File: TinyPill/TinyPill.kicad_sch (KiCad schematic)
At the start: 25 parts

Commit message: Finish GPIO selection
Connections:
- net UART_TX: now reaches U?.12 (PA2)
- net UART_RX: now reaches U?.13 (PA3)
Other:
- note added: "MCU and USB-C 2.0"
- note added: "Power Supply"
- note added: "TinyPill"
- company: (none) -> John Trachte
- title: (none) -> TinyPill Schematic
- moved on the sheet: C?, D?, FB?, J?, R?, SW?, U?

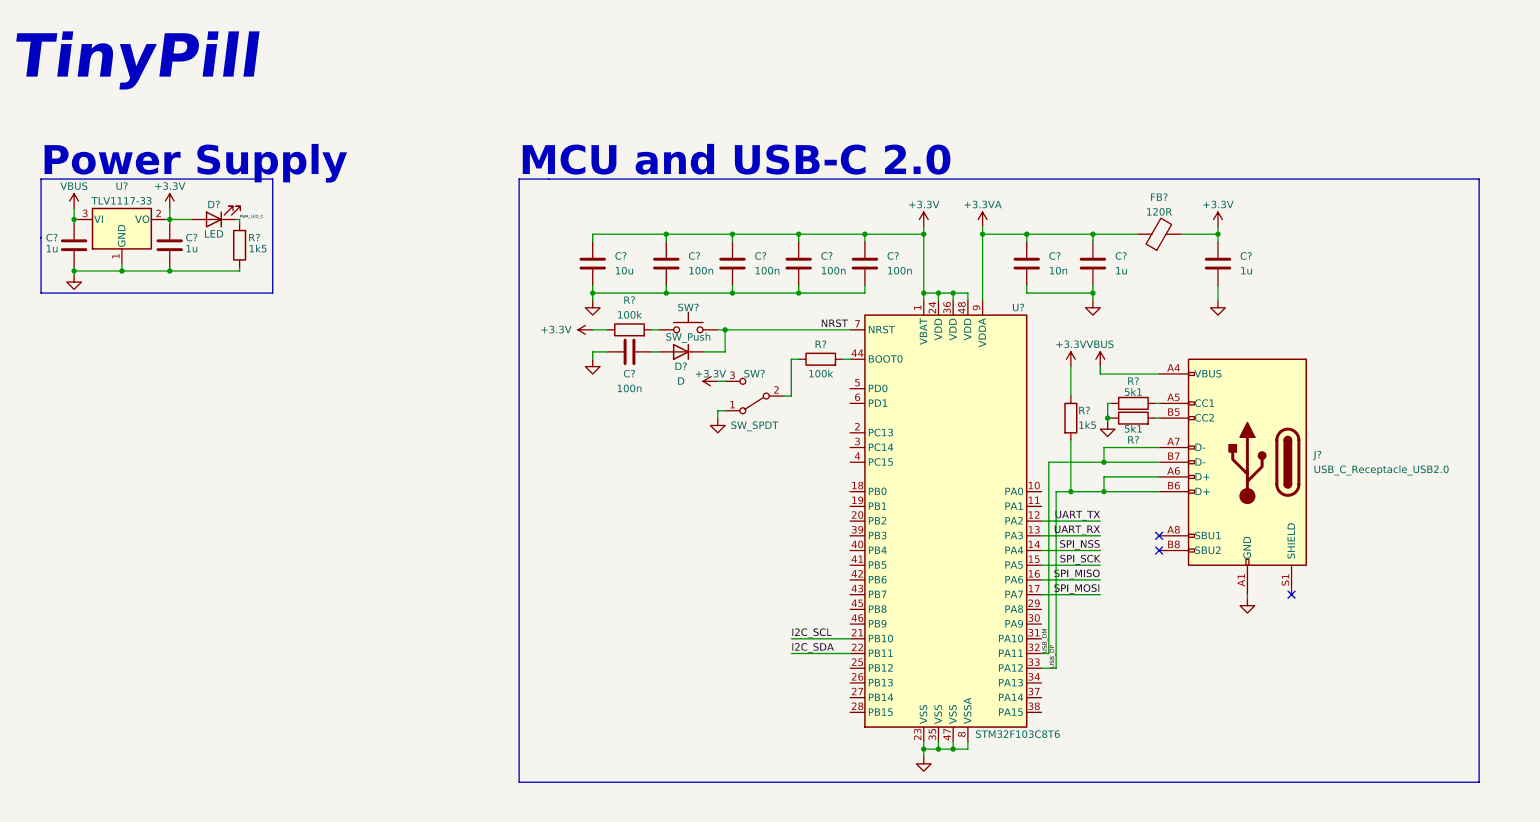
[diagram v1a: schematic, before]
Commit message: Annotations, footprint assignment
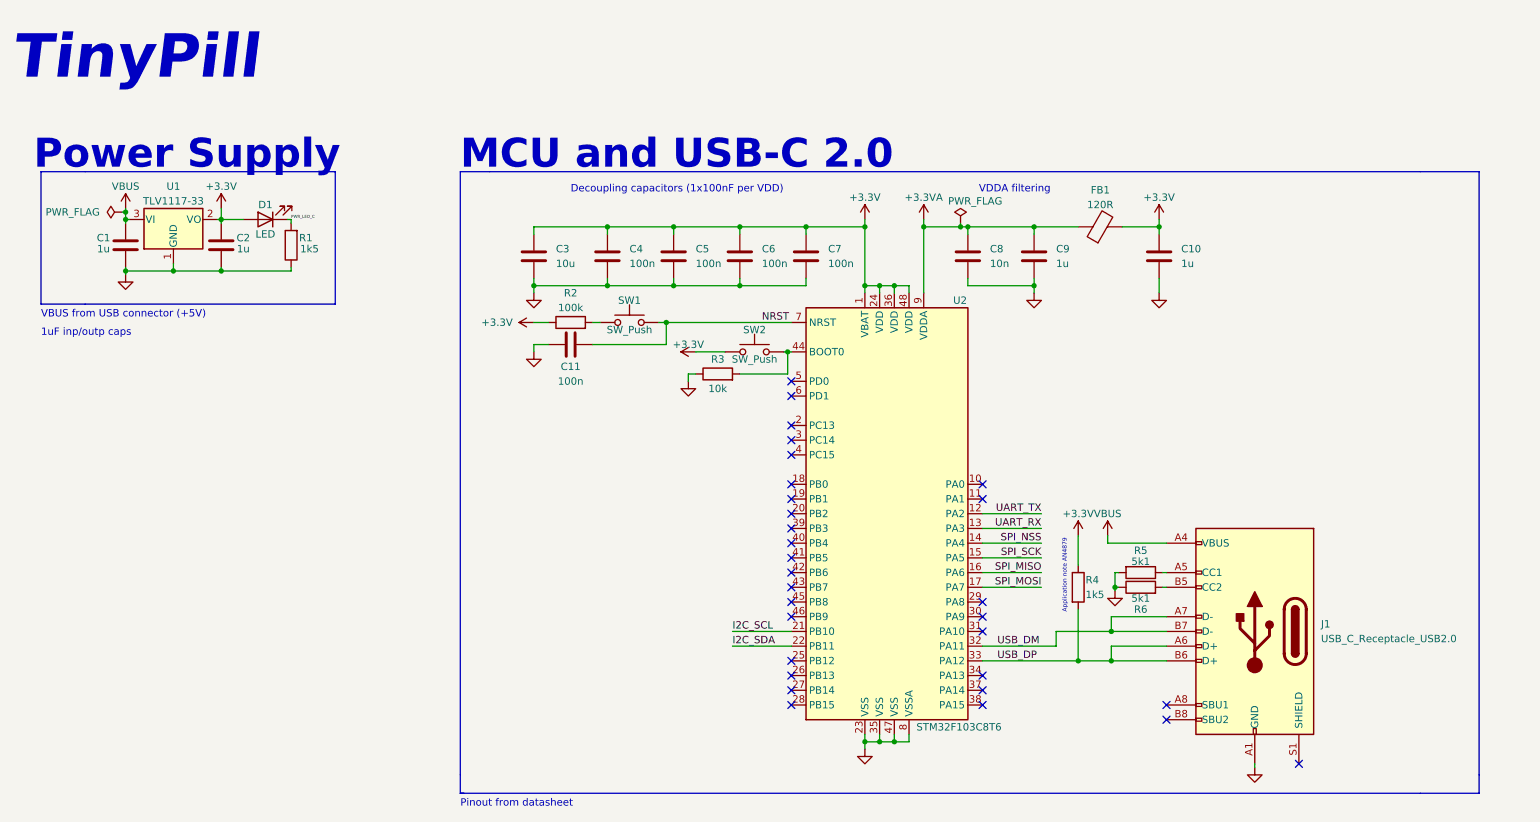
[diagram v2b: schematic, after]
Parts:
- removed D?: D, symbol Device:D
- removed SW?: SW_SPDT, symbol Switch:SW_SPDT
- added SW2: SW_Push, Button_Switch_SMD:SW_DIP_SPSTx01_Slide_Omron_A6S-110x_W8.9mm_P2.54mm, symbol Switch:SW_Push
- C1, C10, C2, C3, C9: renamed from C?; footprint (none) -> Capacitor_SMD:C_0603_1608Metric
- C11, C4, C5, C6, C7, C8: renamed from C?; footprint (none) -> Capacitor_SMD:C_0402_1005Metric
- D1: renamed from D?; footprint (none) -> LED_SMD:LED_0603_1608Metric
- FB1: renamed from FB?; footprint (none) -> Inductor_SMD:L_0603_1608Metric
- J1: renamed from J?; footprint (none) -> Connector_USB:USB_C_Receptacle_Palconn_UTC16-G
- R1, R2, R4: renamed from R?; footprint (none) -> Resistor_SMD:R_0402_1005Metric
- R3: renamed from R?; value 100k -> 10k; footprint (none) -> Resistor_SMD:R_0402_1005Metric
- R5, R6: renamed from R?; footprint (none) -> Resistor_SMD:R_0603_1608Metric
- SW1: renamed from SW?; footprint (none) -> Button_Switch_SMD:SW_Push_SPST_NO_Alps_SKRK
- U1: renamed from U?; footprint (none) -> Package_TO_SOT_SMD:SOT-223-3_TabPin2
- gave numbers to parts that had none: 1
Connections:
- net +3V3: now also SW2.1
- net GND: now also R3.1
- net NRST: now also C11.1
- net at R3.2, U2.44 (BOOT0): now also SW2.2
- no-connect marks 3 -> 30
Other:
- note added: "1uF inp/outp caps"
- note added: "Application note AN4879"
- note added: "Decoupling capacitors (1x100nF per VDD)"
- note added: "Pinout from datasheet"
- note added: "VBUS from USB connector (+5V)"
- note added: "VDDA filtering"
- moved on the sheet: C1, C10, C11, C2, C3, C4, C5, C6, C7, C8, C9, D1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

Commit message: Initial layout, begin routing
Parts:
- added R7, R8: 1k5, Resistor_SMD:R_0402_1005Metric, symbol Device:R
- J1: footprint Connector_USB:USB_C_Receptacle_Palconn_UTC16-G -> Connector_USB:USB_C_Receptacle_GCT_USB4085
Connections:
- net +3V3: now also R7.2, R8.2
- net I2C_SCL: now also R7.1
- net I2C_SDA: now also R8.1
- net USB_DM renamed USB_D-
- net USB_DP renamed USB_D+
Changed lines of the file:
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@@
   (junction (at 168.91 144.78) (diameter 0) (color 0 0 0 0)
+  )
+  (junction (at 139.065 116.205) (diameter 0) (color 0 0 0 0)
   )
   (junction (at 156.21 55.88) (diameter 0) (color 0 0 0 0)
@@
     (stroke (width 0) (type default) (color 0 0 0 0))
   )
+  (wire (pts (xy 139.065 116.205) (xy 142.24 116.205))
+    (stroke (width 0) (type default) (color 0 0 0 0))
+  )
   (wire (pts (xy 109.22 66.04) (xy 109.22 67.31))
     (stroke (width 0) (type default) (color 0 0 0 0))
@@
     (stroke (width 0) (type default) (color 0 0 0 0))
   )
-  (wire (pts (xy 153.67 125.73) (xy 143.51 125.73))
+  (wire (pts (xy 142.24 125.73) (xy 153.67 125.73))
     (stroke (width 0) (type default) (color 0 0 0 0))
   )
@@
     (stroke (width 0) (type default) (color 0 0 0 0))
   )
+  (wire (pts (xy 139.065 119.38) (xy 139.065 116.205))
+    (stroke (width 0) (type default) (color 0 0 0 0))
+  )
   (wire (pts (xy 130.81 72.39) (xy 132.08 72.39))
     (stroke (width 0) (type default) (color 0 0 0 0))
@@
     (stroke (width 0) (type default) (color 0 0 0 0))
   )
+  (wire (pts (xy 153.67 128.27) (xy 139.065 128.27))
+    (stroke (width 0) (type default) (color 0 0 0 0))
+  )
   (wire (pts (xy 182.88 55.245) (xy 182.88 55.88))
     (stroke (width 0) (type default) (color 0 0 0 0))
@@
     (stroke (width 0) (type default) (color 0 0 0 0))
   )
+  (wire (pts (xy 139.065 128.27) (xy 139.065 127))
+    (stroke (width 0) (type default) (color 0 0 0 0))
+  )
   (wire (pts (xy 109.22 76.2) (xy 111.76 76.2))
     (stroke (width 0) (type default) (color 0 0 0 0))
@@
     (stroke (width 0) (type default) (color 0 0 0 0))
   )
+  (wire (pts (xy 142.24 124.46) (xy 142.24 125.73))
+    (stroke (width 0) (type default) (color 0 0 0 0))
+  )
   (wire (pts (xy 166.37 54.61) (xy 166.37 55.88))
     (stroke (width 0) (type default) (color 0 0 0 0))
@@
     (stroke (width 0) (type default) (color 0 0 0 0))
   )
+  (wire (pts (xy 139.065 115.57) (xy 139.065 116.205))
+    (stroke (width 0) (type default) (color 0 0 0 0))
+  )
   (wire (pts (xy 38.735 62.865) (xy 38.735 63.5))
     (stroke (width 0) (type default) (color 0 0 0 0))
@@
     (stroke (width 0) (type default) (color 0 0 0 0))
   )
+  (wire (pts (xy 142.24 116.205) (xy 142.24 116.84))
+    (stroke (width 0) (type default) (color 0 0 0 0))
+  )
   (polyline (pts (xy 262.255 153.67) (xy 96.52 153.67))
     (stroke (width 0) (type default) (color 0 0 0 0))
@@
   )
   (wire (pts (xy 195.58 57.15) (xy 195.58 55.88))
-    (stroke (width 0) (type default) (color 0 0 0 0))
-  )
-  (wire (pts (xy 143.51 128.27) (xy 153.67 128.27))
     (stroke (width 0) (type default) (color 0 0 0 0))
   )
@@
     (effects (font (size 1.27 1.27)) (justify left bottom))
   )
-  (label "USB_DM" (at 189.23 128.27 0)
+  (label "USB_D-" (at 189.23 128.27 0)
     (effects (font (size 1.27 1.27)) (justify left bottom))
   )
@@
     (effects (font (size 1.27 1.27)) (justify right bottom))
   )
-  (label "USB_DP" (at 189.23 130.81 0)
+  (label "USB_D+" (at 189.23 130.81 0)
     (effects (font (size 1.27 1.27)) (justify left bottom))
   )
@@
     (pin "2")
   )
+  (symbol (lib_id "power:+3.3V") (at 139.065 115.57 0) (unit 1)
+    (in_bom yes) (on_board yes)
+    (property "Reference" "#PWR0101" (id 0) (at 139.065 119.38 0)
+      (effects (font (size 1.27 1.27)) hide)
+    )
+    (property "Value" "+3.3V" (id 1) (at 139.065 111.76 0))
+    (property "Footprint" "" (id 2) (at 139.065 115.57 0)
+      (effects (font (size 1.27 1.27)) hide)
+    )
+    (property "Datasheet" "" (id 3) (at 139.065 115.57 0)
+      (effects (font (size 1.27 1.27)) hide)
+    )
+    (pin "1")
+  )
   (symbol (lib_id "Device:LED") (at 62.865 54.61 180) (unit 1)
     (in_bom yes) (on_board yes)
@@
     (pin "2")
   )
+  (symbol (lib_id "Device:R") (at 142.24 120.65 180) (unit 1)
+    (in_bom yes) (on_board yes)
+    (property "Reference" "R7" (id 0) (at 144.78 119.38 0))
+    (property "Value" "1k5" (id 1) (at 145.415 121.285 0))
+    (property "Footprint" "Resistor_SMD:R_0402_1005Metric" (id 2) (at 144.018 120.65 90)
+      (effects (font (size 1.27 1.27)) hide)
+    )
+    (property "Datasheet" "~" (id 3) (at 142.24 120.65 0)
+      (effects (font (size 1.27 1.27)) hide)
+    )
+    (pin "1")
+    (pin "2")
+  )
   (symbol (lib_id "Device:R") (at 203.2 118.11 0) (unit 1)
     (in_bom yes) (on_board yes)
@@
     )
     (property "Datasheet" "~" (id 3) (at 38.735 59.055 0)
+      (effects (font (size 1.27 1.27)) hide)
+    )
+    (pin "1")
+    (pin "2")
+  )
+  (symbol (lib_id "Device:R") (at 139.065 123.19 180) (unit 1)
+    (in_bom yes) (on_board yes)
+    (property "Reference" "R8" (id 0) (at 135.255 121.92 0))
+    (property "Value" "1k5" (id 1) (at 135.89 123.825 0))
+    (property "Footprint" "Resistor_SMD:R_0402_1005Metric" (id 2) (at 140.843 123.19 90)
+      (effects (font (size 1.27 1.27)) hide)
+    )
+    (property "Datasheet" "~" (id 3) (at 139.065 123.19 0)
       (effects (font (size 1.27 1.27)) hide)
     )
@@
       (effects (font (size 1.27 1.27)) (justify right))
     )
-    (property "Footprint" "Connector_USB:USB_C_Receptacle_Palconn_UTC16-G" (id 2) (at 229.87 125.73 0)
+    (property "Footprint" "Connector_USB:USB_C_Receptacle_GCT_USB4085" (id 2) (at 229.87 125.73 0)
       (effects (font (size 1.27 1.27)) hide)
     )
@@
       (reference "#PWR018") (unit 1) (value "GND") (footprint "")
     )
+    (path "/092a7123-8c90-408c-98ab-589321f60edd"
+      (reference "#PWR0101") (unit 1) (value "+3.3V") (footprint "")
+    )
     (path "/80d25750-dcb7-42d1-99fc-d8e207e54007"
       (reference "C1") (unit 1) (value "1u") (footprint "Capacitor_SMD:C_0603_1608Metric")
@@
     )
     (path "/eb84fba5-7e27-4fee-8ac8-868fe1e2089b"
-      (reference "J1") (unit 1) (value "USB_C_Receptacle_USB2.0") (footprint "Connector_USB:USB_C_Receptacle_Palconn_UTC16-G")
+      (reference "J1") (unit 1) (value "USB_C_Receptacle_USB2.0") (footprint "Connector_USB:USB_C_Receptacle_GCT_USB4085")
     )
     (path "/b14712a4-9c9e-48c0-be8f-ce6bdf09f871"
@@
       (reference "R6") (unit 1) (value "5k1") (footprint "Resistor_SMD:R_0603_1608Metric")
     )
+    (path "/7b100f60-553d-4d07-adb9-494f507c847d"
+      (reference "R7") (unit 1) (value "1k5") (footprint "Resistor_SMD:R_0402_1005Metric")
+    )
+    (path "/8364b0dc-5de7-4ae0-a284-9af7333dc9c8"
+      (reference "R8") (unit 1) (value "1k5") (footprint "Resistor_SMD:R_0402_1005Metric")
+    )
     (path "/6a81b78d-1908-4613-a02c-4d93820cdb96"

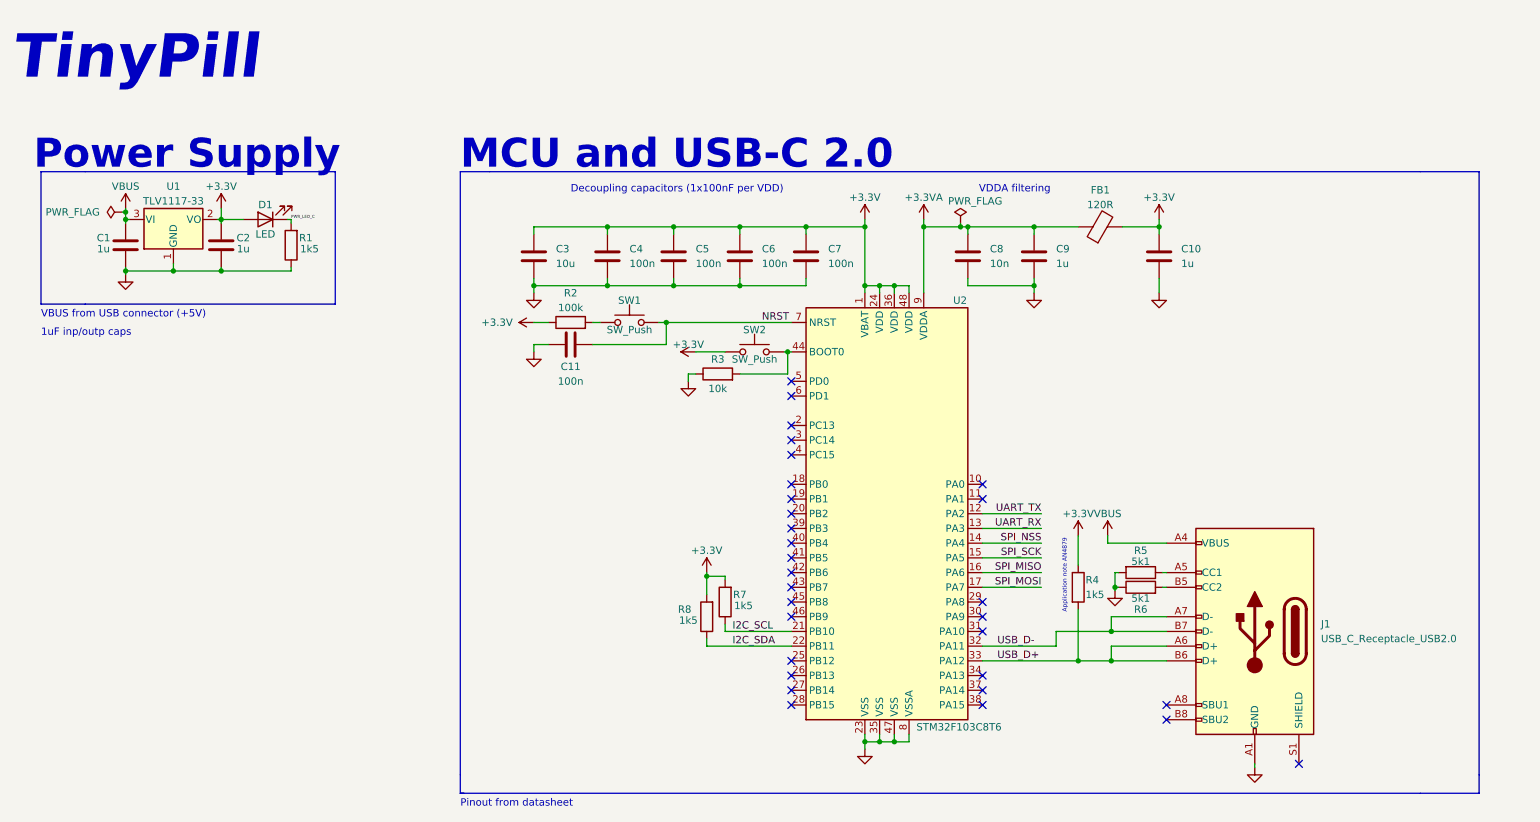
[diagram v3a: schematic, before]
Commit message: Change USB C port to USB B Micro to support smaller board footprint
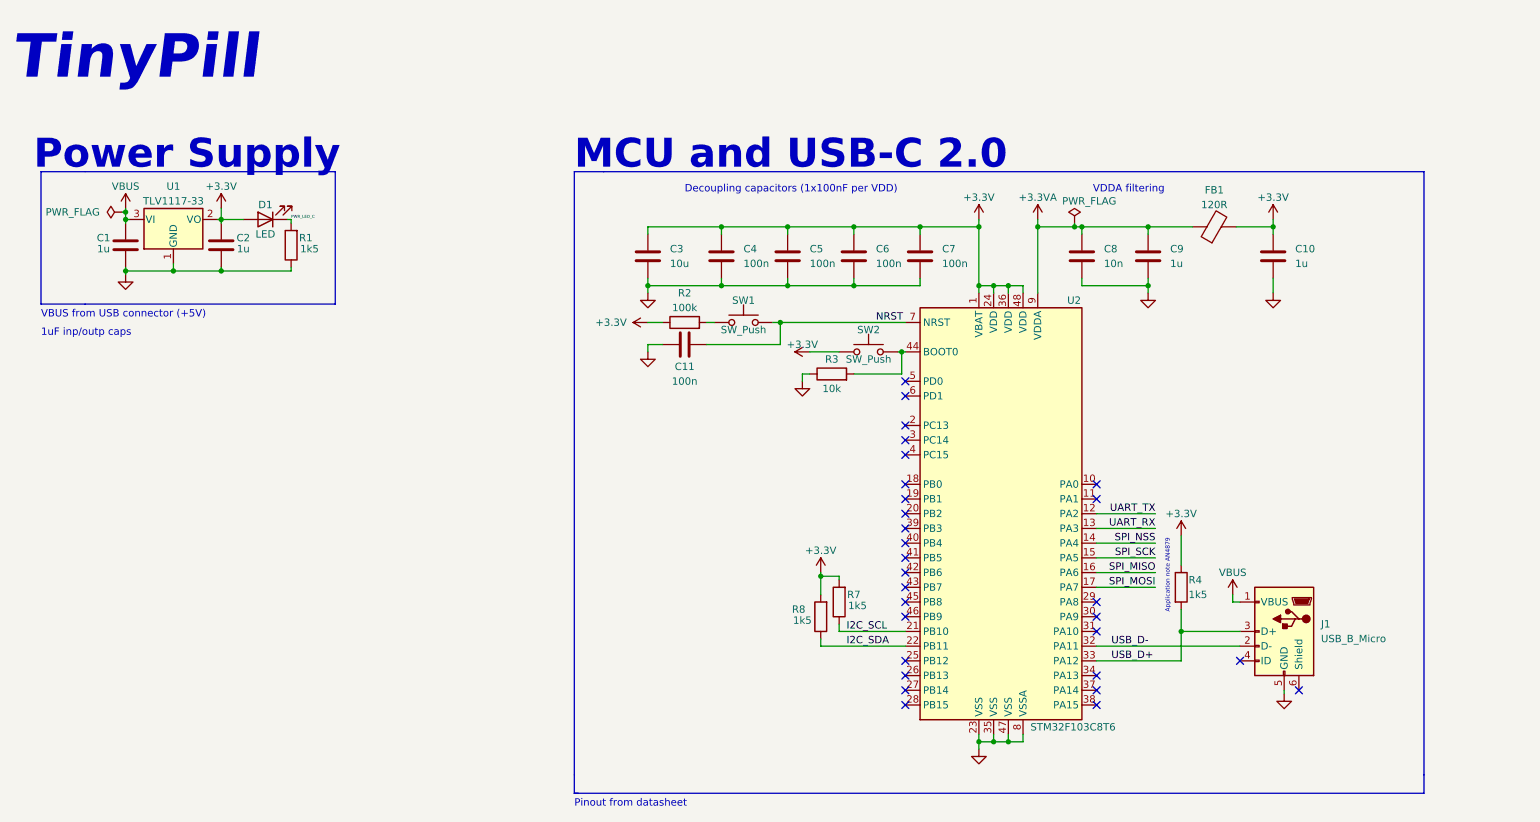
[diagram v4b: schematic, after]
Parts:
- removed J1: USB_C_Receptacle_USB2.0, Connector_USB:USB_C_Receptacle_GCT_USB4085, symbol Connector:USB_C_Receptacle_USB2.0
- removed R5, R6: 5k1, Resistor_SMD:R_0603_1608Metric, symbol Device:R
- added J1: USB_B_Micro, symbol Connector:USB_B_Micro
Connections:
- net GND: now also J1.5 (GND)
- net USB_D+: now also J1.3 (D+)
- net USB_D-: now also J1.2 (D-)
- net VBUS: now also J1.1 (VBUS)
- no-connect marks 30 -> 29
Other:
- moved on the sheet: C10, C11, C3, C4, C5, C6, C7, C8, C9, FB1, R2, R3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
